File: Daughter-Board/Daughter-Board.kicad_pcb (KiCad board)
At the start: 2 copper layers, 116 parts, among them J201 302-S101, J301 Conn_01x08_0.5mm_Female_Kyoce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, J401 Conn_01x08_0.5mm_Female_Kyoce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, J501 Conn_01x08_0.5mm_Female_Kyoce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, J601 Conn_01x08_0.5mm_Female_Kyoce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, P101 EdgeConn, P102 EdgeConn, U101 LMV934MA, U102 LM324A, U103 4016, U104 4016, U105 4016, U106 MC74VHCT126A, U107 MC74VHCT126A, U108 4016, U109 4016, U201 74HC540, U202 PIC32MZ2048EFM064-TQFP

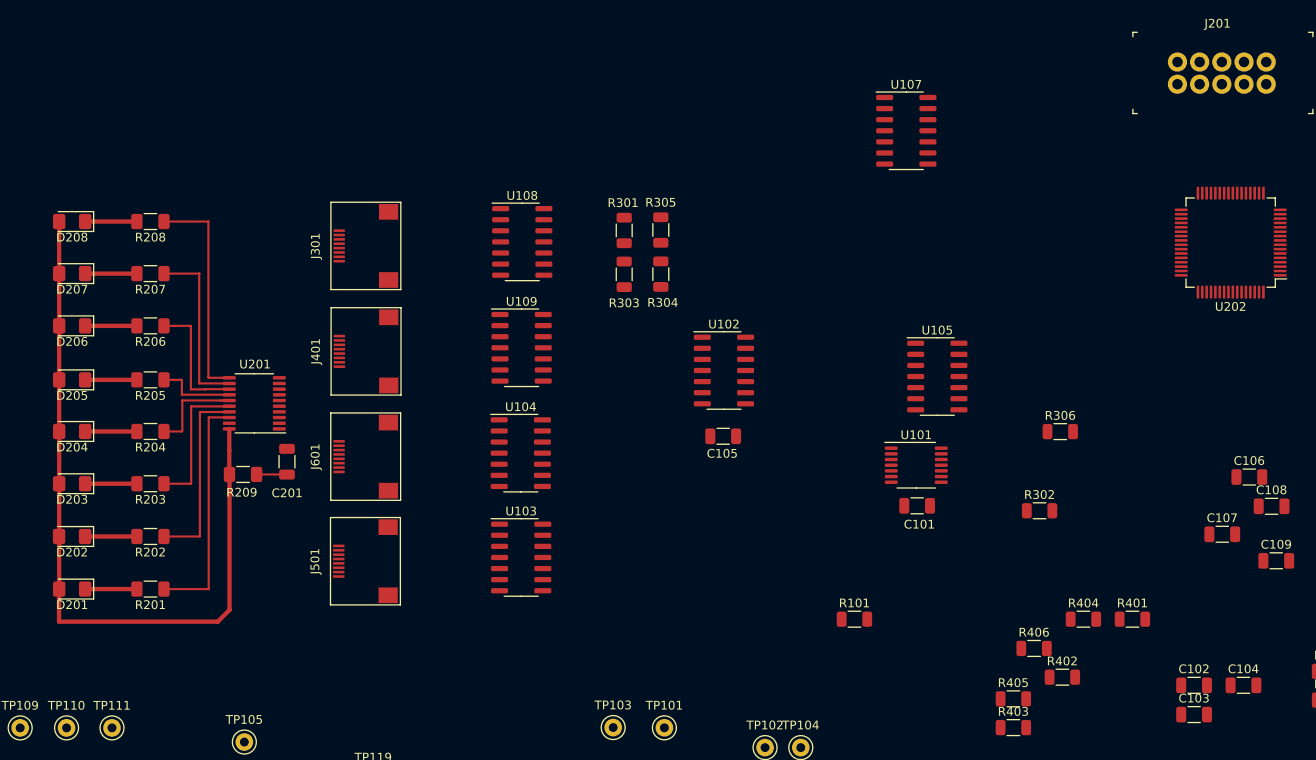
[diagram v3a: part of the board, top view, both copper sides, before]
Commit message: Remove LEDs and circuitry, update J201 footprint to have a square pad on pin 1.]
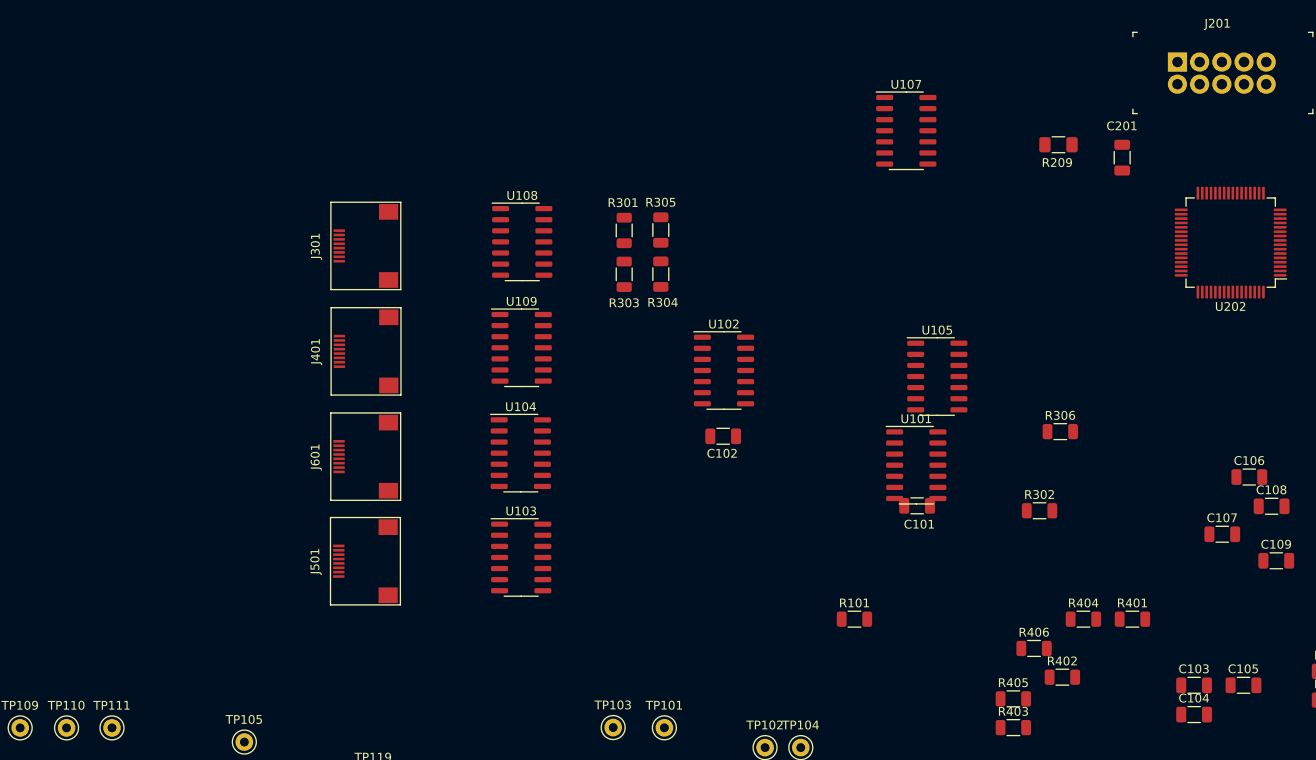
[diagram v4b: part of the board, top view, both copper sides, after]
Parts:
- removed D201, D202, D203, D204, D205, D206, D207, D208: LED_ALT, LED_SMD:LED_1206_3216Metric_Pad1.42x1.75mm_HandSolder
- removed R201, R202, R203, R204, R205, R206, R207, R208: 1.0K, Resistor_SMD:R_1206_3216Metric_Pad1.30x1.75mm_HandSolder
- removed U201: 74HC540, Package_SO:TSSOP-20_4.4x6.5mm_P0.65mm
- U101: footprint Package_SO:TSSOP-14_4.4x5mm_P0.65mm -> Package_SO:SOIC-14_3.9x8.7mm_P1.27mm
- U103, U104, U105, U108, U109: value 4016 -> 74HC4016
- moved C201 101.7 mm to (16.6, -106.2), turned to 270 degrees
- moved R209 100.7 mm to (9.30, -107.7)
- renumbered C105 to C102, C102 to C103, C103 to C104, C104 to C105
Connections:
- net /Digital/No_Gain renamed /Digital/SingleGain
- R302 pad 2: /Digital/PlusEn -> PlusEn
- R306 pad 2: /Digital/Plus_GND -> Plus_GND
- R402 pad 2: /Digital/PlusEn -> PlusEn
- R406 pad 2: /Mic_Interface_2/Plus_GND -> Plus_GND
- R502 pad 2: /Mic_Interface_4/PlusEn -> PlusEn
- R506 pad 2: /Digital/Plus_GND -> Plus_GND
- R602 pad 2: /Digital/PlusEn -> PlusEn
- R606 pad 2: /Digital/Plus_GND -> Plus_GND
- TP202 pad 1: /Digital/Plus_GND -> Plus_GND
- TP204 pad 1: /Digital/PlusEn -> PlusEn
- U103 pad 13: /Mic_Interface_4/PlusEn -> PlusEn
- U103 pad 5: /Digital/Plus_GND -> Plus_GND
- U104 pad 13: /Digital/PlusEn -> PlusEn
- U104 pad 5: /Digital/Plus_GND -> Plus_GND
- U105 pad 1: /Mic_Interface_1/AOut -> Net-(R304-Pad1)
- U105 pad 10: Net-(R604-Pad2) -> GNDREF
- U105 pad 11: /Mic_Interface_3/AOut -> Net-(R604-Pad1)
- U105 pad 2: Net-(R304-Pad2) -> GNDREF
- U105 pad 3: Net-(R404-Pad2) -> GNDREF
- U105 pad 4: /Mic_Interface_2/AOut -> Net-(R404-Pad1)
- U105 pad 8: /Mic_Interface_4/AOut -> Net-(R504-Pad1)
- U105 pad 9: Net-(R504-Pad2) -> GNDREF
- U108 pad 13: /Digital/PlusEn -> PlusEn
- U108 pad 5: /Digital/Plus_GND -> Plus_GND
- U109 pad 13: /Digital/PlusEn -> PlusEn
- U109 pad 5: /Mic_Interface_2/Plus_GND -> Plus_GND
- U202 pad 52: /Digital/Mic1 -> Net-(U202-Pad52)
- U202 pad 53: /Digital/Mic2 -> Net-(U202-Pad53)
- U202 pad 56: /Digital/Mic3 -> Net-(U202-Pad56)
- U202 pad 57: /Digital/Mic4 -> Net-(U202-Pad57)
- U202 pad 61: /Digital/PlusEn -> PlusEn
- U202 pad 63: /Digital/Plus_GND -> Plus_GND
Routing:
- net +5V: track 86.6 -> 0.00 mm
- net Net-(R201-Pad1): track 27.1 -> 0.00 mm
- net /Digital/Y7: track 25.3 -> 0.00 mm
- net /Digital/Y1: track 21.7 -> 0.00 mm
- net Net-(R207-Pad1): track 20.1 -> 0.00 mm
- net Net-(R203-Pad1): track 16.3 -> 0.00 mm
- net /Digital/Y5: track 14.8 -> 0.00 mm
- net /Digital/Y3: track 11.0 -> 0.00 mm
- net Net-(R205-Pad1): track 9.18 -> 0.00 mm
- net Net-(D202-Pad1): track 5.93 -> 0.00 mm
- net Net-(D208-Pad1): track 5.92 -> 0.00 mm
- net Net-(D207-Pad1): track 5.92 -> 0.00 mm
- net Net-(D206-Pad1): track 5.92 -> 0.00 mm
- net Net-(D205-Pad1): track 5.92 -> 0.00 mm
- net Net-(D204-Pad1): track 5.92 -> 0.00 mm
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
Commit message: Add connector for PICkit to MCU interface.
In the process of adding the PICkit connector some control lines had to be moved.
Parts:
- removed U202: PIC32MZ2048EFM064-TQFP, Package_QFP:TQFP-64_10x10mm_P0.5mm
- added J202: TSW-108-09-G-S-RA, SAMTEC_TSW-108-09-G-S-RA, F.Cu at (18.6, -134.2)
- added TP226: 5000, digikey-footprints:Test_Point_D1.02mm, F.Cu at (-18.1, -135.9)
- added TP227: 5000, digikey-footprints:Test_Point_D1.02mm, F.Cu at (-18.1, -131.8)
- added TP228: 5000, digikey-footprints:Test_Point_D1.02mm, F.Cu at (-14.0, -135.9)
- added TP229: 5000, digikey-footprints:Test_Point_D1.02mm, F.Cu at (-14.0, -131.8)
- added TP230: 5000, digikey-footprints:Test_Point_D1.02mm, F.Cu at (-9.93, -135.9)
- added U201: PIC32MZ2048EFM064-TQFP, Package_QFP:TQFP-64_10x10mm_P0.5mm, F.Cu at (-28.6, -121.2)
- R209: value 3.9K -> 10K
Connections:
- net Net-(C201-Pad1) renamed /Digital/~MCLR
- net Net-(J201-Pad2) renamed /Digital/TMS
- net Net-(J201-Pad4) renamed /Digital/TCK
- net Net-(J201-Pad6) renamed /Digital/TDO
- net Net-(J201-Pad8) renamed /Digital/TDI
- J201 pad 3: Net-(J201-Pad3) -> GNDREF
- J201 pad 5: Net-(J201-Pad3) -> GNDREF
- J201 pad 9: Net-(J201-Pad3) -> GNDREF
- TP216 pad 1: /Mic_Interface_4/AOut -> /Digital/DOut_EN_1
- TP217 pad 1: /Digital/DOut_EN_1 -> /Mic_Interface_4/AOut
- U106 pad 11: Net-(U106-Pad11) -> /Digital/MCLK
- U106 pad 3: Net-(U106-Pad3) -> /Digital/I2S
- U106 pad 6: Net-(U106-Pad6) -> /Digital/I2C
- U106 pad 8: Net-(U106-Pad8) -> /Digital/SPI

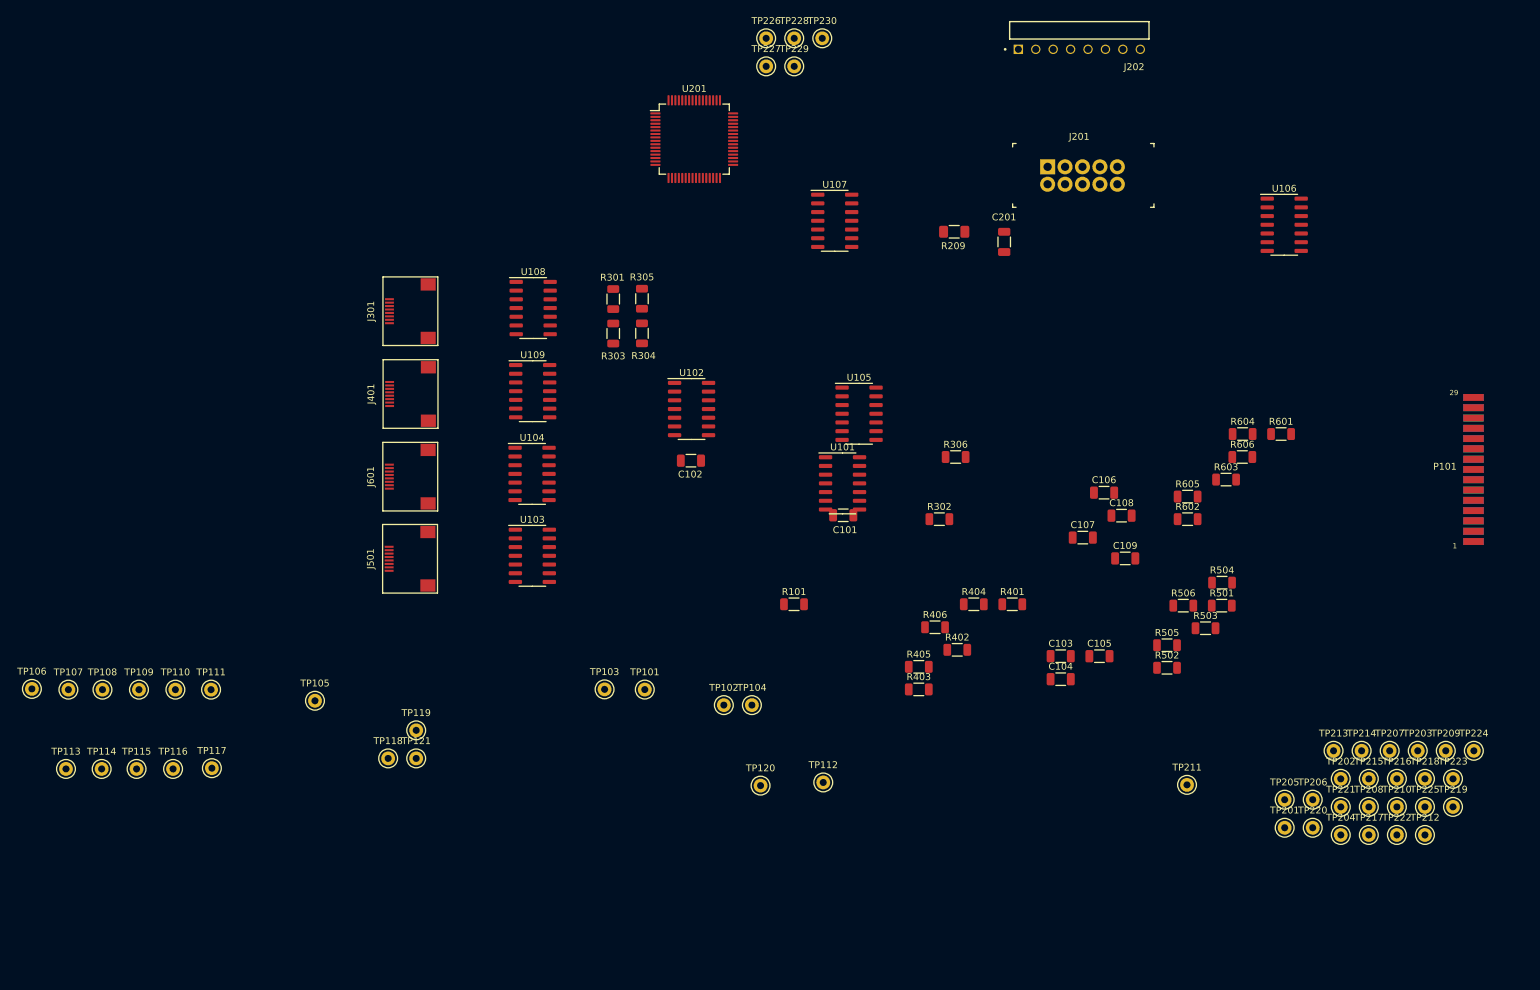
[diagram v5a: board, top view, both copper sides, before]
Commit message: Modify schematic to recover PCB layout.
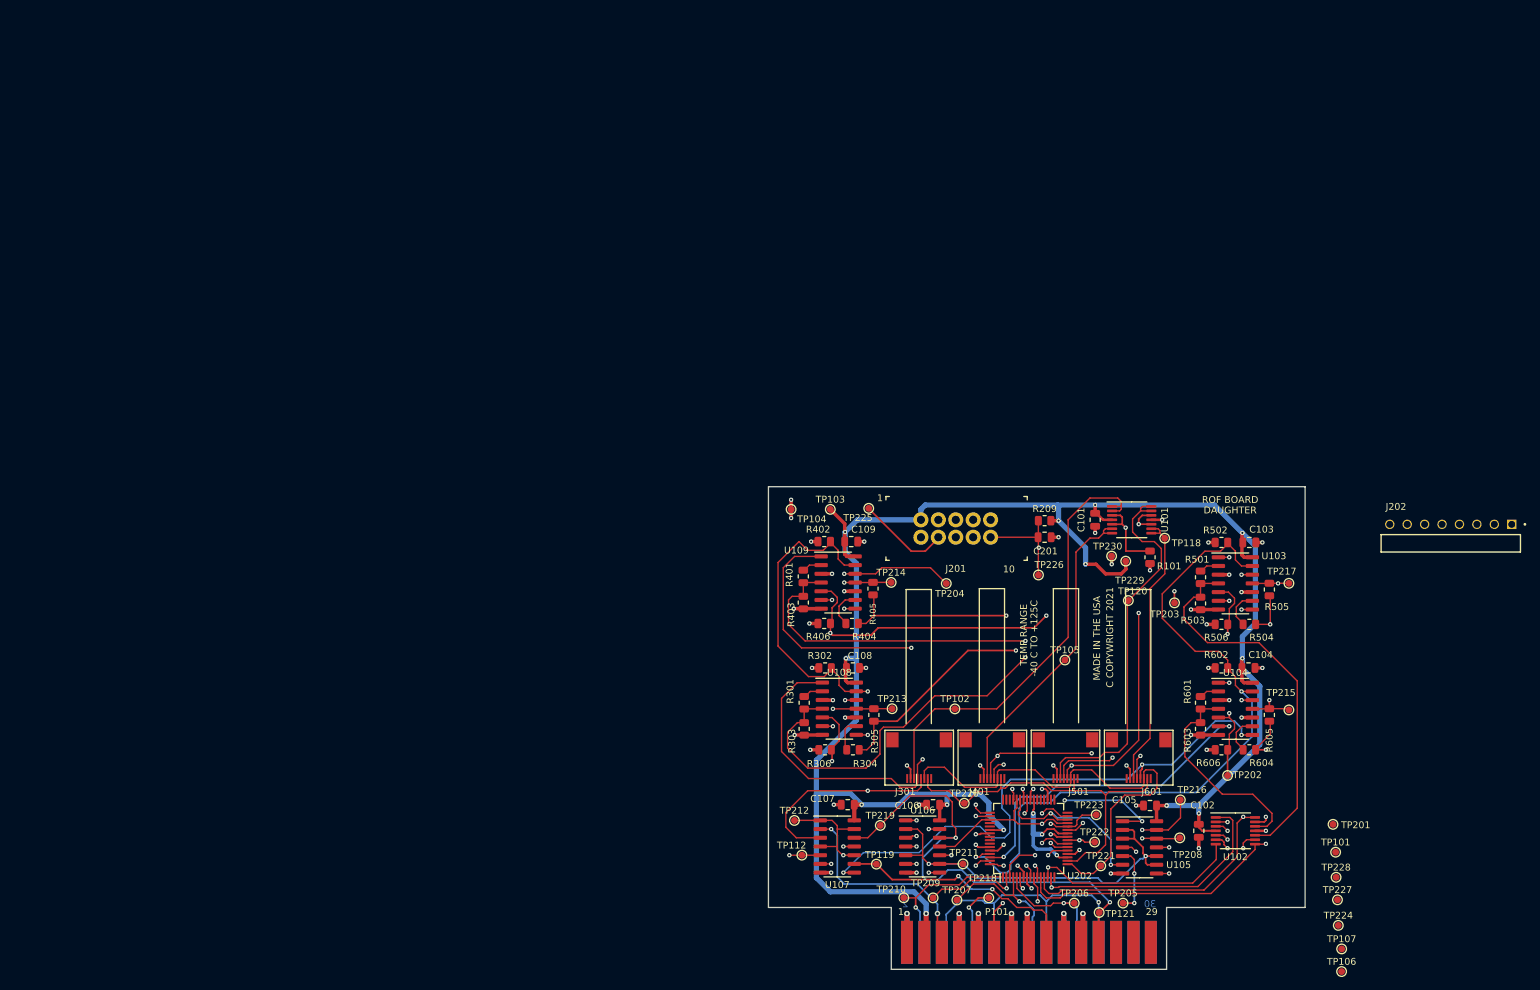
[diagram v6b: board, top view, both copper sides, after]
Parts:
- removed TP108, TP109, TP110, TP111, TP113, TP114, TP115, TP116, TP117: 5000, digikey-footprints:Test_Point_D1.02mm
- removed U201: PIC32MZ2048EFM064-TQFP, Package_QFP:TQFP-64_10x10mm_P0.5mm
- added U202: PIC32MZ2048EFM064-TQFP, Package_QFP:TQFP-64_10x10mm_P0.5mm, F.Cu at (20.2, -19.2)
- C101, C102, C103, C104, C105, C106, C107, C108, C109, C201: footprint Capacitor_SMD:C_1206_3216Metric -> Capacitor_SMD:C_0805_2012Metric
- R101, R301, R302, R303, R304, R305, R306, R401, R402, R403, R404, R405, R406, R501, R502, R503, R504, R505, R506, R601, R602, R603, R604, R605, R606: footprint Resistor_SMD:R_1206_3216Metric -> Resistor_SMD:R_0805_2012Metric
- R209: footprint Resistor_SMD:R_1206_3216Metric_Pad1.30x1.75mm_HandSolder -> Resistor_SMD:R_0805_2012Metric
- TP101, TP102, TP103, TP104, TP105, TP106, TP107, TP112, TP118, TP119, TP120, TP121, TP201, TP202, TP203, TP204, TP205, TP206, TP207, TP208, TP209, TP210, TP211, TP212, TP213, TP214, TP215, TP216, TP217, TP218, TP219, TP220, TP221, TP222, TP223, TP224, TP225, TP226, TP227, TP228, TP229, TP230: footprint digikey-footprints:Test_Point_D1.02mm -> TestPoint:TestPoint_Pad_D1.0mm
- U101, U102: footprint Package_SO:SOIC-14_3.9x8.7mm_P1.27mm -> Package_SO:TSSOP-14_4.4x5mm_P0.65mm
- moved TP106 195.3 mm to (65.8, 0.20)
- moved TP107 189.4 mm to (65.8, -3.10)
- moved TP227 147.3 mm to (65.2, -10.3)
- moved TP228 145.6 mm to (65.0, -13.5)
- moved TP118 117.7 mm to (40.0, -63.0)
- moved J601 113.8 mm to (36.2, -31.0), turned to 180 degrees
- moved TP105 109.5 mm to (25.4, -45.2)
- moved U104 108.1 mm to (50.3, -38.1)
- moved U106 104.8 mm to (4.70, -18.0)
- moved TP101 103.5 mm to (64.9, -17.2)
- moved U103 102.6 mm to (50.3, -56.4)
- moved TP121 102.1 mm to (30.4, -8.41)
- moved U102 100.3 mm to (50.3, -20.3)
- moved J401 100.0 mm to (14.9, -31.0), turned to 180 degrees
- moved J501 99.9 mm to (25.5, -31.0), turned to 180 degrees
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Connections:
- net /Digital/MST_CLK renamed /MIC_MST_CLK_4
- net /Mic_Interface_1/AOut renamed /AOut_1
- net /Mic_Interface_1/MST_CLK renamed /MIC_MST_CLK_1
- net /Mic_Interface_1/V_Bias renamed /V_BIAS_1
- net /Mic_Interface_2/AOut renamed /AOut_2
- net /Mic_Interface_2/MST_CLK renamed /MIC_MST_CLK_2
- net /Mic_Interface_2/V_Bias renamed /V_BIAS_2
- net /Mic_Interface_3/AOut renamed /AOut_3
- net /Mic_Interface_3/MST_CLK renamed /MIC_MST_CLK_3
- net /Mic_Interface_3/V_Bias renamed /V_BIAS_3
- net /Mic_Interface_4/AOut renamed /AOut_4
- net /Mic_Interface_4/V_Bias renamed /V_BIAS_4
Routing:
- net PlusEn: track 0.00 -> 398.2 mm, vias 0 -> 8
- net +5V: track 0.00 -> 363.5 mm, vias 0 -> 21
- net Plus_GND: track 0.00 -> 175.7 mm, vias 0 -> 6
- net /MST_Bias: track 0.00 -> 163.4 mm, vias 0 -> 3
- net /Digital/NegEn: track 0.00 -> 158.0 mm, vias 0 -> 6
- net /Mic_Interface_2/AOut: track 0.00 -> 125.7 mm, vias 0 -> 2
- net /Mic_Interface_1/AOut: track 0.00 -> 112.3 mm, vias 0 -> 2
- net GNDREF: track 0.00 -> 111.2 mm, vias 0 -> 50
- net /Digital/~MCLR: track 0.00 -> 106.6 mm, vias 0 -> 2
- net Net-(J501-Pad5): track 0.00 -> 99.9 mm, vias 0 -> 4
- net Net-(R301-Pad1): track 0.00 -> 97.3 mm, vias 0 -> 2
- net Net-(J401-Pad4): track 0.00 -> 95.4 mm, vias 0 -> 4
- net Net-(J501-Pad4): track 0.00 -> 93.5 mm, vias 0 -> 3
- net Net-(R401-Pad1): track 0.00 -> 93.3 mm, vias 0 -> 2
- net /Mic_Interface_4/AOut: track 0.00 -> 84.9 mm, vias 0 -> 2
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- added copper zone on In1.Cu, net GNDREF
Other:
- board outline added: 78.2 x 70.4 mm
- copper layers 2 -> 4
- rule pad_to_mask_clearance: 0 -> 0.127
- rule trace_min: 0.2 -> 0.2032
- rule via_min_size: 0.4 -> 0.635
- board text added: "-40 C TO +125C"
- board text added: "10"
- board text added: "C COPYWRIGHT 2021"
- board text added: "DAUGHTER"
- board text added: "MADE IN THE USA"
- board text added: "ROF BOARD"
- board text added: "TEMP RANGE"
